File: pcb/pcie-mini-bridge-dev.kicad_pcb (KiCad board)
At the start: 4 copper layers, 75.4 x 23.5 mm, 24 parts, among them J1 Conn_01x02, J2 USB_C_Receptacle, J3 Conn_01x02, J4 Conn_01x02, J5 PCIe_x1, U1 TPS2594xx

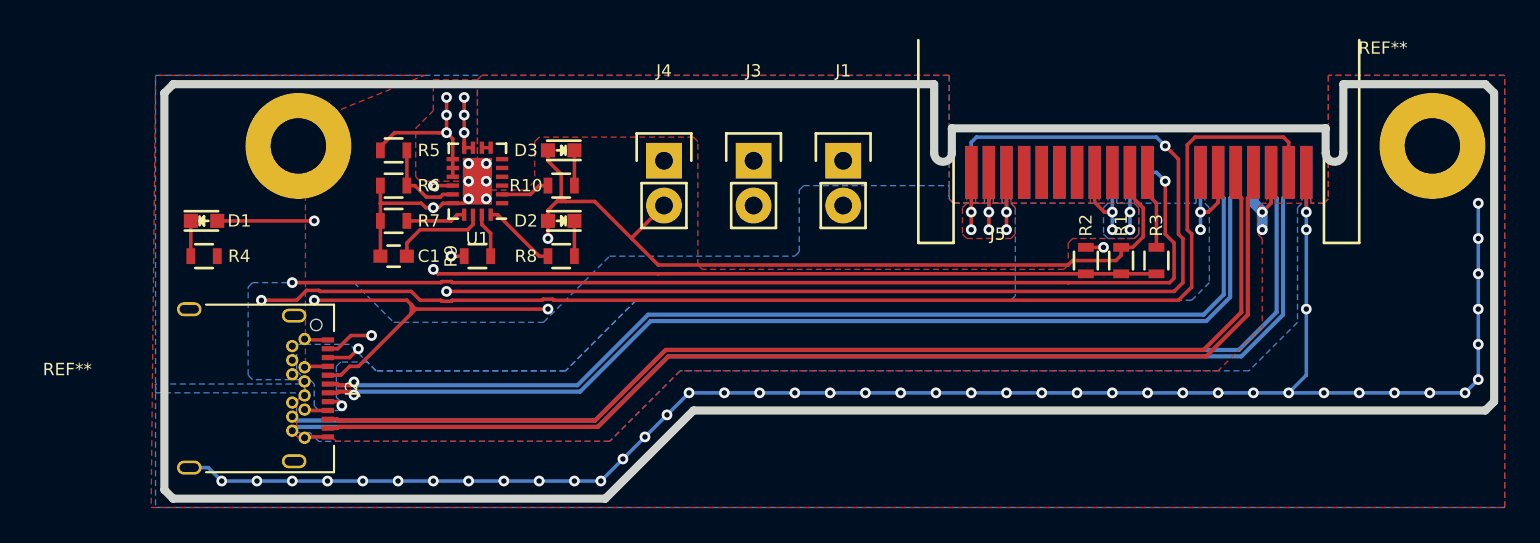
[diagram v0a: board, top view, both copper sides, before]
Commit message: fix drc and dfm problems and make rev 1 gerbers
* fix usb c recp. drc. change suggested .7/.4mm th/drills to .6728/.368mm th/drills to meet 6mil annular rings and 5mil spacing. remove slots.
* clean up silk, add board labels
* fix soldermask sizing to .051mm clearance with .077mm min width
* remove PCIe length matching on host board because host + dev is correct length
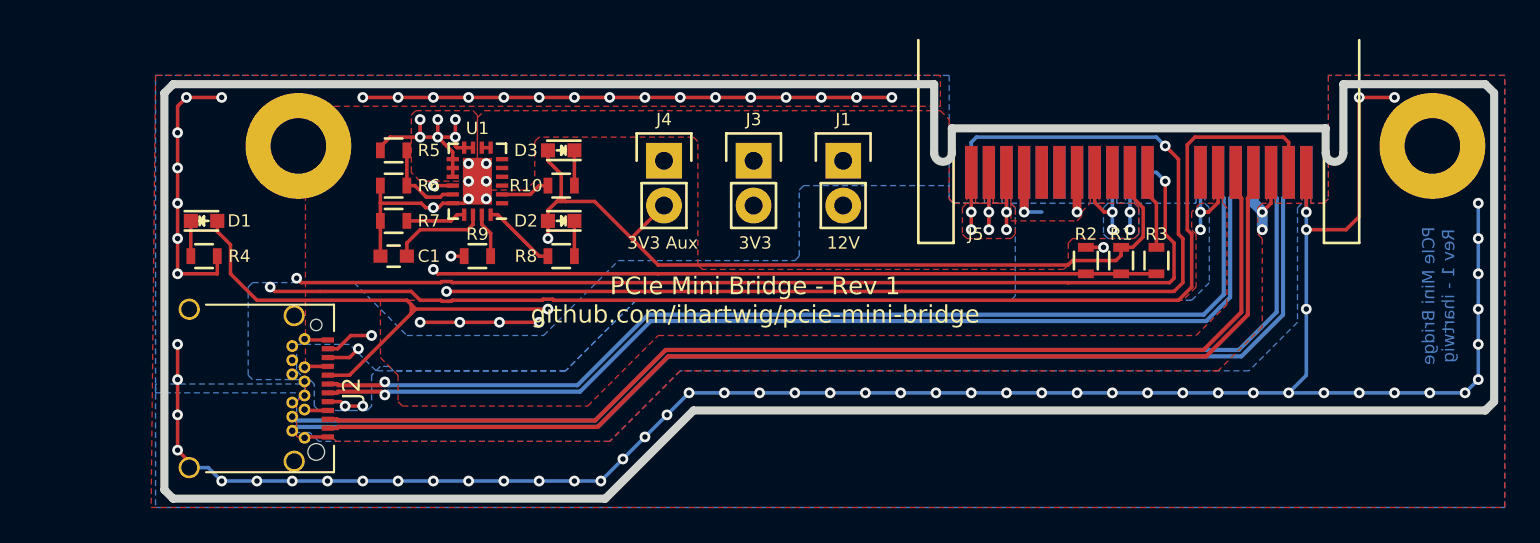
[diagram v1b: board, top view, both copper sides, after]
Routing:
- net GND: track 131.1 -> 223.5 mm, vias 60 -> 95
- net /PE_3V3_AUX: track 83.0 -> 81.7 mm, vias 4 -> 2
- net +12V: track 15.1 -> 16.3 mm, vias 7 -> 8
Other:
- net class PCIe Data: via_dia 0.7 -> 0.6096; via_drill 0.4 -> 0.3048
- rule pad_to_mask_clearance: 0 -> 0.051
- board text added: "12V"
- board text added: "3V3"
- board text added: "3V3 Aux"
- board text added: "PCIe Mini Bridge - Rev 1 github.com/ihartwig/pcie-mini-bridge"
- board text added: "PCIe Mini Bridge Rev 1 - ihartwig"

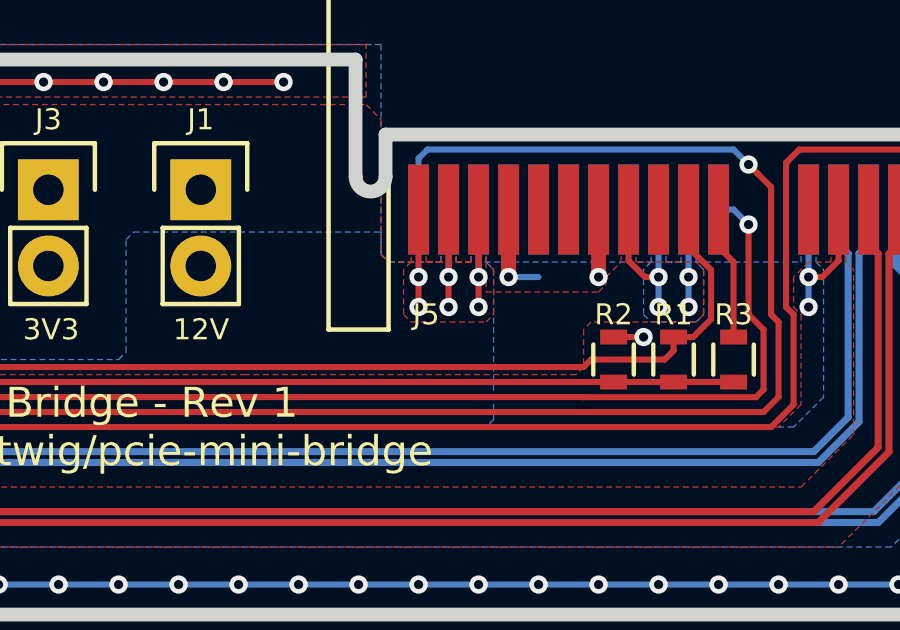
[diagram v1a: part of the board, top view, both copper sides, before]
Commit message: fix pcie footprints and remove paste and update gerbers
* fix PCIe_Fingers and PCIe_SMDEdge had bottom cu with top mask/paste
* make and use PCIe_SMDEdge-NoPaste_TE_5-1734857-x
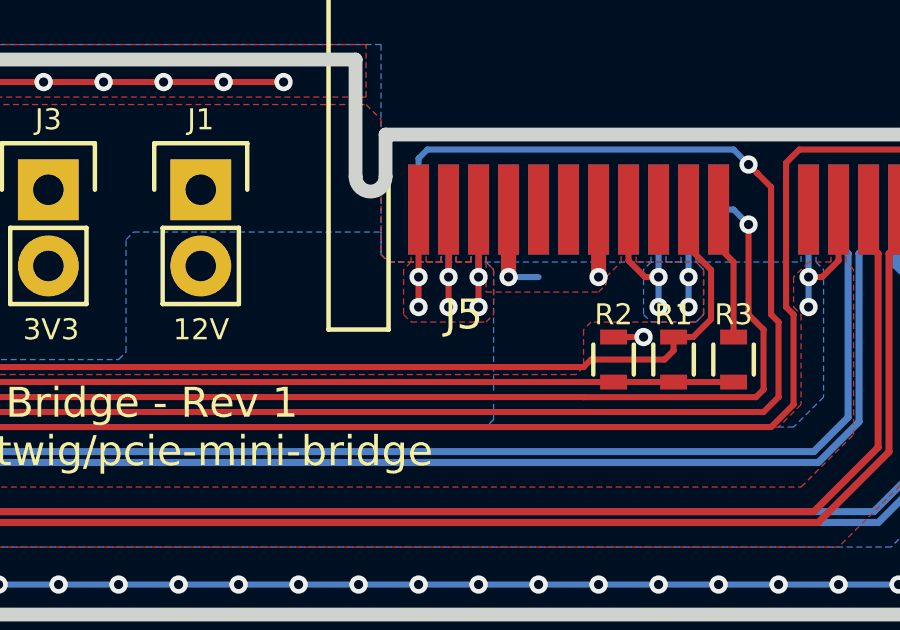
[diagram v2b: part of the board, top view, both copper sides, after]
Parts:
- J5: footprint pcie-mini-bridge-special:PCIe_SMDEdge_TE_5-1734857-x -> pcie-mini-bridge-special:PCIe_SMDEdge-NoPaste_TE_5-1734857-x
- R10, R4, R8: value 220 -> 1k
